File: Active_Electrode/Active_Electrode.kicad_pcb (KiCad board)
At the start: 2 copper layers, 14 parts, among them J1 Conn_01x02, J2 Conn_01x09, U1 ADG442BNZ, U2 LF412

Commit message: Active Electrode
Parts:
- moved C9 0.25 mm to (7.87, 21.1)
- moved C10 0.25 mm to (5.08, 18.5)

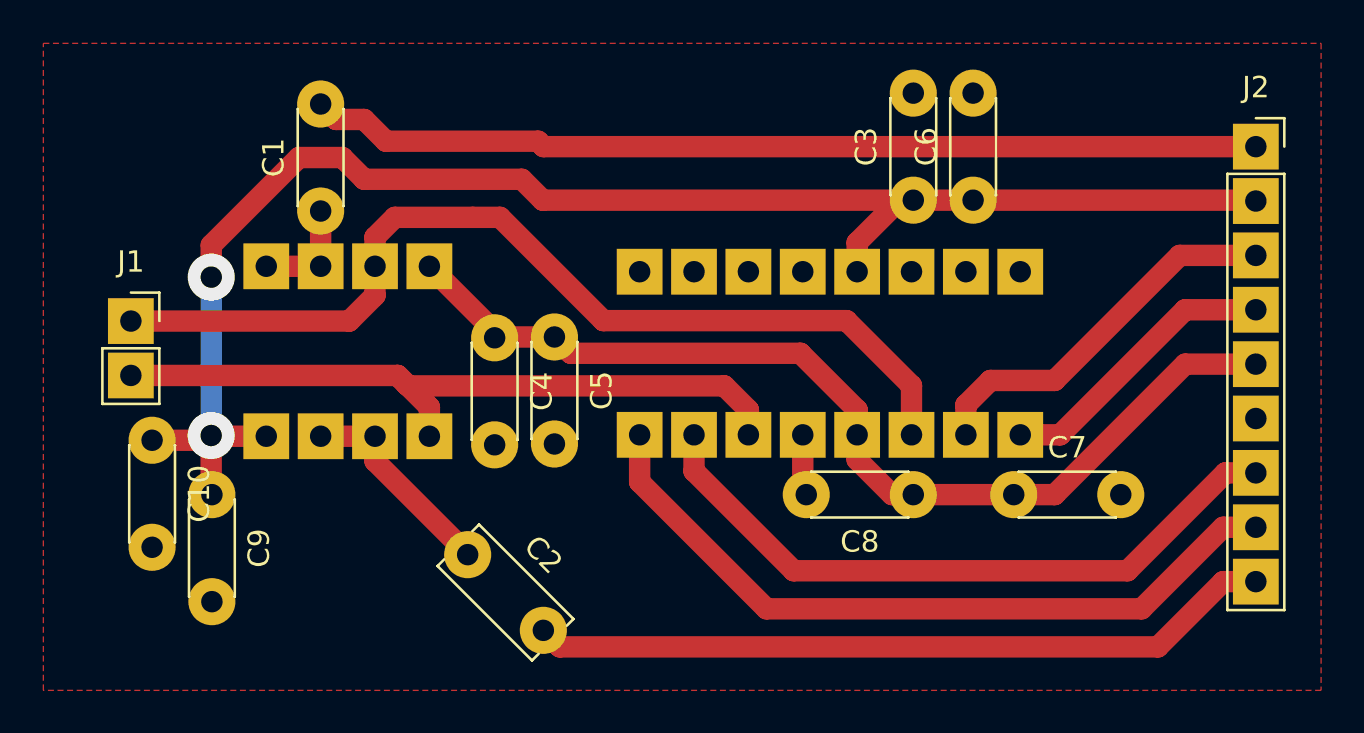
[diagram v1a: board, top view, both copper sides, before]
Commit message: Modularize control script
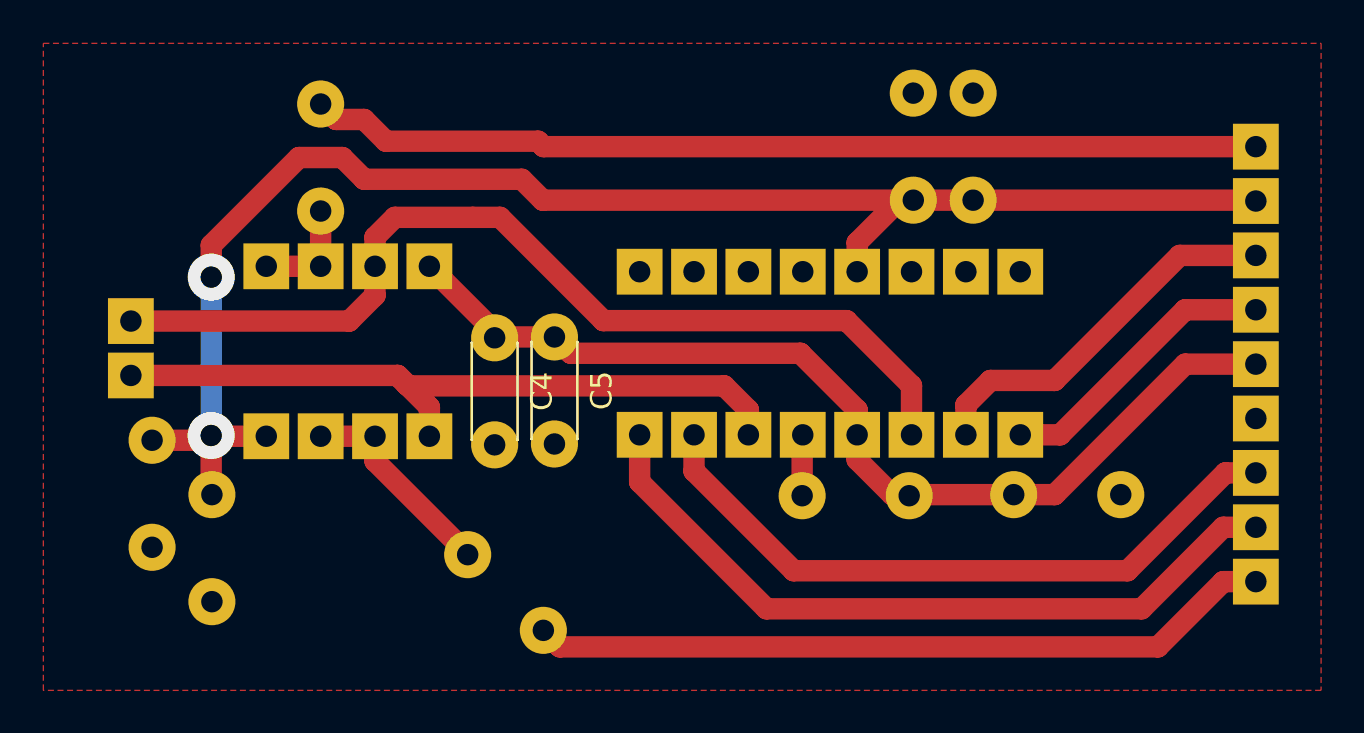
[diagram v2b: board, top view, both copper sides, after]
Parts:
- C1, C10, C2, C3, C6, C7, C8, C9, J1, J2: moved to B.Cu
- moved C8 0.20 mm to (40.4, 21.1)
- turned J1 to 180 degrees
- turned J2 to 180 degrees

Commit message: Mill Digital Select breakout board and more active electrodes
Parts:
- U2: value LF412 -> LF412CN
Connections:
- net /+15V renamed /+12V
- net /-15V renamed /-12V
- net Net-(U2-NEG_A) renamed /Neg1_Feedback
- net Net-(U2-NEG_B) renamed /Neg2_FeedBack

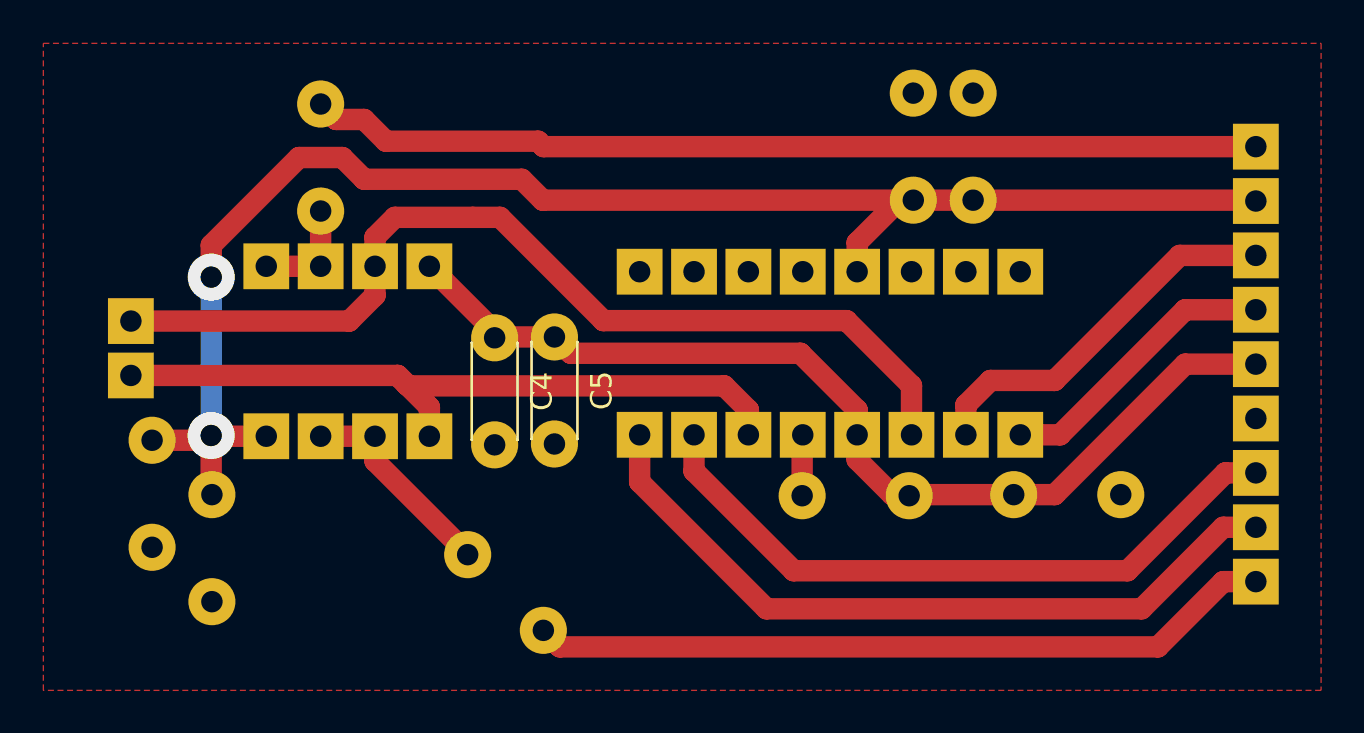
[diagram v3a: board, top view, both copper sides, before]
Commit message: Corrections made to active electrode and made 2 more
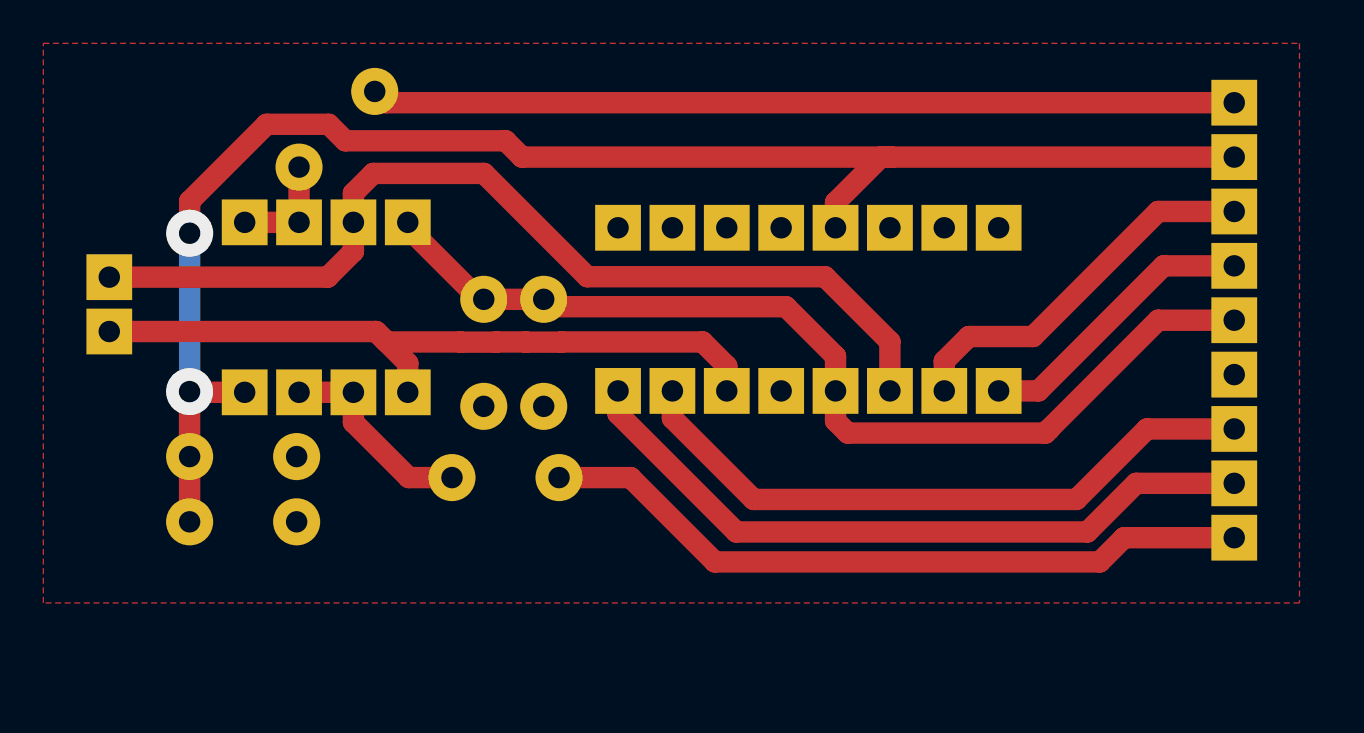
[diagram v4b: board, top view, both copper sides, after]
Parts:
- removed C3, C4: C, Capacitor_THT:C_Disc_D4.3mm_W1.9mm_P5.00mm
- removed C5, C6: C_Polarized, Capacitor_THT:C_Disc_D4.3mm_W1.9mm_P5.00mm
- C1, C2: value C -> 1µ
- C10, C8: value C -> 1n
- C7, C9: value C_Polarized -> 1µ
- moved C7 23.8 mm to (23.4, 12.0), turned to -90 degrees
- moved C8 21.9 mm to (20.6, 12.0), turned to -90 degrees
- moved C2 3.67 mm to (19.1, 20.3), turned to 0 degrees
- moved C1 2.29 mm to (11.9, 5.78), turned to 45 degrees
- moved J1 2.29 mm to (3.08, 10.9)
- moved J2 2.29 mm to (55.6, 2.77)
- moved U1 2.29 mm to (44.6, 16.2)
- moved U2 2.29 mm to (13.2, 12.3)
- moved C10 1.91 mm to (6.83, 19.3), turned to 0 degrees
- moved C9 1.64 mm to (6.83, 22.4), turned to 0 degrees
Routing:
- net /ADC_CH1: track 44.5 -> 40.4 mm
- net GND: track 2.86 -> 0.04 mm
- net /DigiSelect2: track 35.0 -> 33.1 mm
- net /CURR_CH2: track 31.8 -> 30.5 mm
- net /ADC_CH2: track 34.9 -> 33.6 mm

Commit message: Updated active electrode and other boards
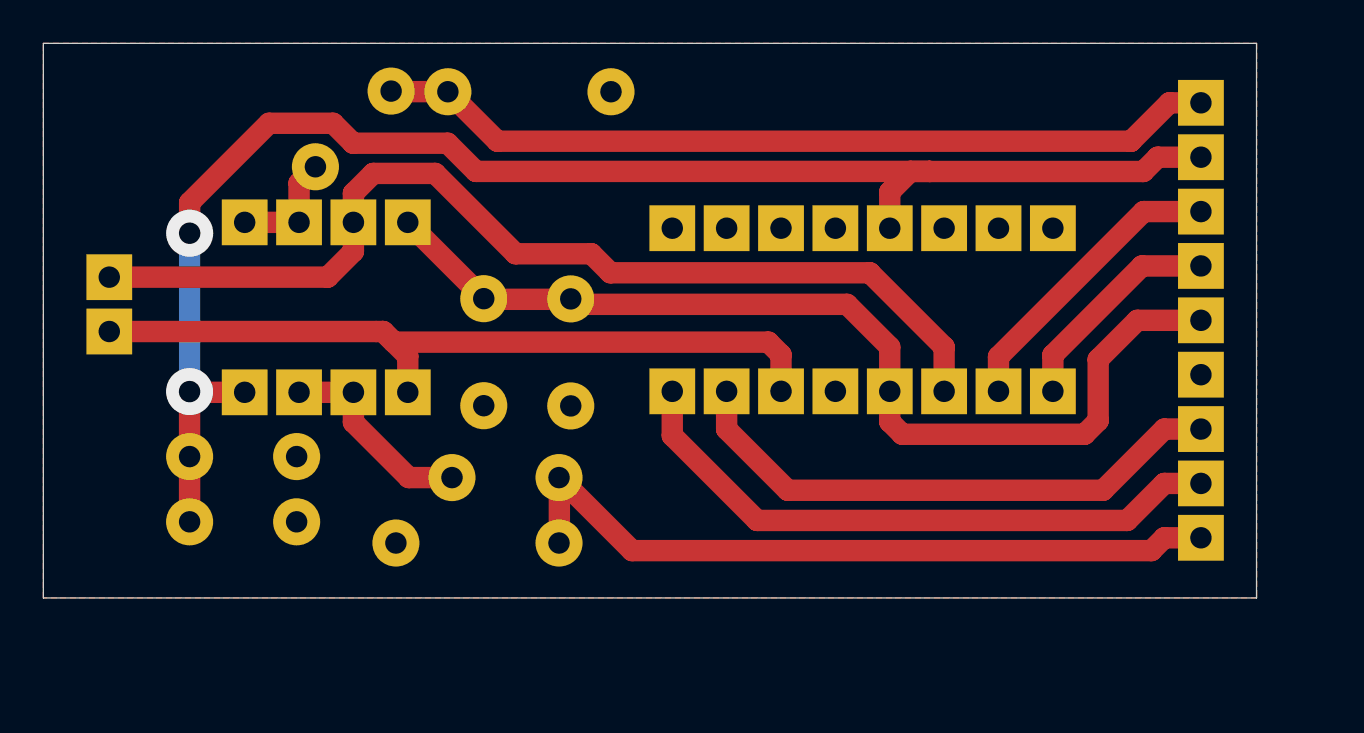
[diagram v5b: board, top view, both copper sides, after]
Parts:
- added R1: 27 kΩ, Resistor_THT:R_Axial_DIN0207_L6.3mm_D2.5mm_P7.62mm_Horizontal, B.Cu at (24.1, 23.3)
- added R2: 27 kΩ, Resistor_THT:R_Axial_DIN0207_L6.3mm_D2.5mm_P7.62mm_Horizontal, B.Cu at (18.9, 2.26)
- C1, C2: value 1µ -> 10n
- C7, C9: footprint Capacitor_THT:C_Disc_D4.3mm_W1.9mm_P5.00mm -> Capacitor_THT:CP_Radial_Tantal_D5.5mm_P5.00mm
- C8: footprint Capacitor_THT:C_Disc_D4.3mm_W1.9mm_P5.00mm -> Capacitor_THT:C_Disc_D6.0mm_W2.5mm_P5.00mm
- moved U1 2.53 mm to (47.2, 16.3)
- moved J2 1.56 mm to (54.1, 2.78)
- moved C7 1.26 mm to (24.6, 11.9)
- moved C1 0.77 mm to (12.7, 5.77)
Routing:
- net /CURR_CH2: track 30.5 -> 26.3 mm
- net /DigiSelect2: track 33.1 -> 29.1 mm
- net /CURR_CH1: track 17.8 -> 13.9 mm
- net /DigiSelect1: track 13.4 -> 10.3 mm
- net /CH2: track 34.1 -> 36.9 mm
- net /CH1: track 45.6 -> 48.0 mm
- net /+12V: track 72.9 -> 71.2 mm
- net /ADC_CH2: track 33.6 -> 34.7 mm
- net /ADC_CH1: track 40.4 -> 39.5 mm
- net /-12V: track 46.8 -> 47.4 mm
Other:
- board outline added: 56.7 x 25.9 mm
